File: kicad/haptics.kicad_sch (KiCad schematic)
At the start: 6 parts, among them M401 VG1040003D, U401 DA7280

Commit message: refactor, fix issues, ready for first design
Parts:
- added R504, R505: 10k, symbol Device:R
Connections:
- net PWR: now also R504.1, R505.1
- net SCL: now also R504.2
- net SDA: now also R505.2
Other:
- moved on the sheet: R401

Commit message: essentially finish schematic, start adding footprints, add new footprints
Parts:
- C501: renamed from C401; footprint (none) -> Capacitor_SMD:C_0603_1608Metric_Pad1.08x0.95mm_HandSolder
- R501: renamed from R505; footprint (none) -> Resistor_SMD:R_0603_1608Metric_Pad0.98x0.95mm_HandSolder
- R502: renamed from R504; footprint (none) -> Resistor_SMD:R_0603_1608Metric_Pad0.98x0.95mm_HandSolder
- R503: renamed from R401; footprint (none) -> Resistor_SMD:R_0603_1608Metric_Pad0.98x0.95mm_HandSolder
- TP501: renamed from TP401; footprint (none) -> TestPoint:TestPoint_Pad_D3.0mm
- TP502: renamed from TP402; footprint (none) -> TestPoint:TestPoint_Pad_D3.0mm
- U501: renamed from U401; footprint (none) -> Package_DFN_QFN:QFN-12-1EP_3x3mm_P0.5mm_EP1.65x1.65mm
- renumbered M401 to M501
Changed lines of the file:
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@@
 		(on_board yes)
 		(dnp no)
-		(property "Reference" "TP402"
+		(property "Reference" "TP502"
 			(at 156.972 83.058 90)
 			(effects
@@
 			)
 		)
-		(property "Footprint" ""
+		(property "Footprint" "TestPoint:TestPoint_Pad_D3.0mm"
 			(at 172.72 88.9 0)
 			(effects
@@
 			(project "kicad"
 				(path "/97e37379-fec6-4f0d-82d9-4ea53516bb02/6e1279b2-387a-4a79-8fd5-6fdc8d551df2"
-					(reference "TP402")
+					(reference "TP502")
 					(unit 1)
 				)
@@
 		(on_board yes)
 		(dnp no)
-		(property "Reference" "TP401"
+		(property "Reference" "TP501"
 			(at 156.972 79.248 90)
 			(effects
@@
 			)
 		)
-		(property "Footprint" ""
+		(property "Footprint" "TestPoint:TestPoint_Pad_D3.0mm"
 			(at 172.72 85.09 0)
 			(effects
@@
 			(project "kicad"
 				(path "/97e37379-fec6-4f0d-82d9-4ea53516bb02/6e1279b2-387a-4a79-8fd5-6fdc8d551df2"
-					(reference "TP401")
+					(reference "TP501")
 					(unit 1)
 				)
@@
 		(on_board yes)
 		(dnp no)
-		(property "Reference" "C401"
+		(property "Reference" "C501"
 			(at 114.808 120.65 0)
 			(effects
@@
 			)
 		)
-		(property "Footprint" ""
+		(property "Footprint" "Capacitor_SMD:C_0603_1608Metric_Pad1.08x0.95mm_HandSolder"
 			(at 125.4252 125.73 0)
 			(effects
@@
 			(project "kicad"
 				(path "/97e37379-fec6-4f0d-82d9-4ea53516bb02/6e1279b2-387a-4a79-8fd5-6fdc8d551df2"
-					(reference "C401")
+					(reference "C501")
 					(unit 1)
 				)
@@
 		(on_board yes)
 		(dnp no)
-		(property "Reference" "R505"
+		(property "Reference" "R501"
 			(at 99.06 93.98 0)
 			(effects
@@
 			)
 		)
-		(property "Footprint" ""
+		(property "Footprint" "Resistor_SMD:R_0603_1608Metric_Pad0.98x0.95mm_HandSolder"
 			(at 103.632 95.25 90)
 			(effects
@@
 			(project "kicad"
 				(path "/97e37379-fec6-4f0d-82d9-4ea53516bb02/6e1279b2-387a-4a79-8fd5-6fdc8d551df2"
-					(reference "R505")
+					(reference "R501")
 					(unit 1)
 				)
@@
 		(dnp no)
 		(fields_autoplaced yes)
-		(property "Reference" "#PWR0402"
+		(property "Reference" "#PWR0502"
 			(at 135.89 127 0)
 			(effects
@@
 			(project "kicad"
 				(path "/97e37379-fec6-4f0d-82d9-4ea53516bb02/6e1279b2-387a-4a79-8fd5-6fdc8d551df2"
-					(reference "#PWR0402")
+					(reference "#PWR0502")
 					(unit 1)
 				)
@@
 		(on_board yes)
 		(dnp no)
-		(property "Reference" "R504"
+		(property "Reference" "R502"
 			(at 107.95 91.44 0)
 			(effects
@@
 			)
 		)
-		(property "Footprint" ""
+		(property "Footprint" "Resistor_SMD:R_0603_1608Metric_Pad0.98x0.95mm_HandSolder"
 			(at 112.522 92.71 90)
 			(effects
@@
 			(project "kicad"
 				(path "/97e37379-fec6-4f0d-82d9-4ea53516bb02/6e1279b2-387a-4a79-8fd5-6fdc8d551df2"
-					(reference "R504")
+					(reference "R502")
 					(unit 1)
 				)
@@
 		(dnp no)
 		(fields_autoplaced yes)
-		(property "Reference" "M401"
+		(property "Reference" "M501"
 			(at 154.94 101.5999 0)
 			(effects
@@
 			(project "kicad"
 				(path "/97e37379-fec6-4f0d-82d9-4ea53516bb02/6e1279b2-387a-4a79-8fd5-6fdc8d551df2"
-					(reference "M401")
+					(reference "M501")
 					(unit 1)
 				)
@@
 		(on_board yes)
 		(dnp no)
-		(property "Reference" "R401"
+		(property "Reference" "R503"
 			(at 119.38 87.63 0)
 			(effects
@@
 			)
 		)
-		(property "Footprint" ""
+		(property "Footprint" "Resistor_SMD:R_0603_1608Metric_Pad0.98x0.95mm_HandSolder"
 			(at 123.952 88.9 90)
 			(effects
@@
 			(project "kicad"
 				(path "/97e37379-fec6-4f0d-82d9-4ea53516bb02/6e1279b2-387a-4a79-8fd5-6fdc8d551df2"
-					(reference "R401")
+					(reference "R503")
 					(unit 1)
 				)
@@
 		(on_board yes)
 		(dnp no)
-		(property "Reference" "U401"
+		(property "Reference" "U501"
 			(at 130.81 86.36 0)
 			(effects
@@
 			)
 		)
-		(property "Footprint" ""
+		(property "Footprint" "Package_DFN_QFN:QFN-12-1EP_3x3mm_P0.5mm_EP1.65x1.65mm"
 			(at 128.27 106.68 0)
 			(effects
@@
 			(project "kicad"
 				(path "/97e37379-fec6-4f0d-82d9-4ea53516bb02/6e1279b2-387a-4a79-8fd5-6fdc8d551df2"
-					(reference "U401")
+					(reference "U501")
 					(unit 1)
 				)
@@
 		(dnp no)
 		(fields_autoplaced yes)
-		(property "Reference" "#PWR0401"
+		(property "Reference" "#PWR0501"
 			(at 124.46 132.08 0)
 			(effects
@@
 			(project "kicad"
 				(path "/97e37379-fec6-4f0d-82d9-4ea53516bb02/6e1279b2-387a-4a79-8fd5-6fdc8d551df2"
-					(reference "#PWR0401")
-					(unit 1)
-				)
+					(reference "#PWR0501")
+					(unit 1)
+				)

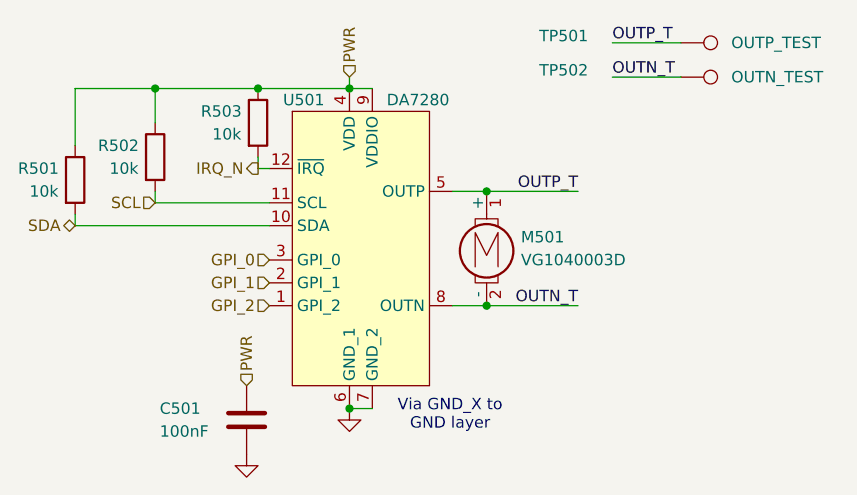
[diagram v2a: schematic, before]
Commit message: fix motor with spring fingers, start PCB
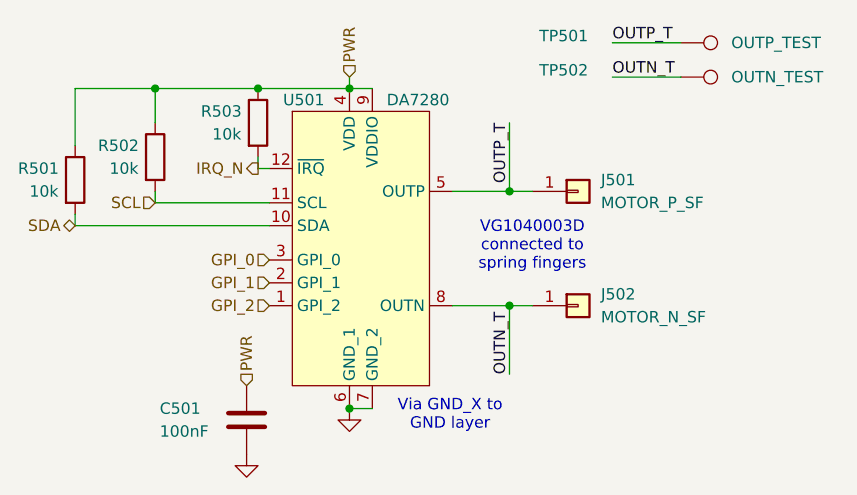
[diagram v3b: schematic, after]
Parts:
- removed M501: VG1040003D, symbol Motor:Motor_DC_ALT
- added J501: MOTOR_P_SF, Raven:TE_2329497-2, symbol Connector_Generic:Conn_01x01
- added J502: MOTOR_N_SF, Raven:TE_2329497-2, symbol Connector_Generic:Conn_01x01
- TP501, TP502: footprint TestPoint:TestPoint_Pad_D3.0mm -> TestPoint:TestPoint_Pad_D1.5mm
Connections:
- net OUTN_T: now also J502.1 (Pin_1)
- net OUTP_T: now also J501.1 (Pin_1)
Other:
- note added: "VG1040003D connected to spring fingers"
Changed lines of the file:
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@@
 	)
 	(junction
-		(at 151.13 109.22)
-		(diameter 0)
-		(color 0 0 0 0)
-	)
-	(junction
-		(at 151.13 96.52)
+		(at 153.67 109.22)
 		(diameter 0)
 		(color 0 0 0 0)
@@
 	)
 	(junction
+		(at 153.67 96.52)
+		(diameter 0)
+		(color 0 0 0 0)
+	)
+	(junction
 		(at 135.89 85.09)
 		(diameter 0)
@@
 	(wire
 		(pts
-			(xy 151.13 109.22) (xy 161.29 109.22)
+			(xy 153.67 109.22) (xy 156.21 109.22)
+		)
+		(stroke
+			(width 0)
+			(type default)
+		)
+	)
+	(wire
+		(pts
+			(xy 153.67 88.9) (xy 153.67 96.52)
 		)
 		(stroke
@@
 	(wire
 		(pts
+			(xy 153.67 109.22) (xy 153.67 116.84)
+		)
+		(stroke
+			(width 0)
+			(type default)
+		)
+	)
+	(wire
+		(pts
 			(xy 135.89 120.65) (xy 138.43 120.65)
 		)
@@
 	(wire
 		(pts
-			(xy 147.32 109.22) (xy 151.13 109.22)
+			(xy 147.32 109.22) (xy 153.67 109.22)
 		)
 		(stroke
@@
 	(wire
 		(pts
-			(xy 147.32 96.52) (xy 151.13 96.52)
+			(xy 147.32 96.52) (xy 153.67 96.52)
 		)
 		(stroke
@@
 	(wire
 		(pts
+			(xy 153.67 96.52) (xy 156.21 96.52)
+		)
+		(stroke
+			(width 0)
+			(type default)
+		)
+	)
+	(wire
+		(pts
 			(xy 105.41 99.06) (xy 105.41 100.33)
 		)
@@
 	(wire
 		(pts
-			(xy 151.13 96.52) (xy 161.29 96.52)
-		)
-		(stroke
-			(width 0)
-			(type default)
-		)
-	)
-	(wire
-		(pts
 			(xy 114.3 88.9) (xy 114.3 85.09)
 		)
@@
 			(width 0)
 			(type default)
+		)
+	)
+	(text "VG1040003D\nconnected to\nspring fingers"
+		(exclude_from_sim no)
+		(at 156.21 102.616 0)
+		(effects
+			(font
+				(size 1.27 1.27)
+			)
 		)
 	)
@@
 	)
 	(label "OUTN_T"
-		(at 161.29 109.22 180)
-		(fields_autoplaced yes)
-		(effects
-			(font
-				(size 1.27 1.27)
-			)
-			(justify right bottom)
+		(at 153.67 116.84 90)
+		(fields_autoplaced yes)
+		(effects
+			(font
+				(size 1.27 1.27)
+			)
+			(justify left bottom)
 		)
 	)
 	(label "OUTP_T"
-		(at 161.29 96.52 180)
+		(at 153.67 88.9 270)
 		(fields_autoplaced yes)
 		(effects
@@
 			)
 			(justify right)
+		)
+	)
+	(symbol
+		(lib_id "Connector_Generic:Conn_01x01")
+		(at 161.29 109.22 0)
+		(unit 1)
+		(exclude_from_sim no)
+		(in_bom yes)
+		(on_board yes)
+		(dnp no)
+		(fields_autoplaced yes)
+		(property "Reference" "J502"
+			(at 163.83 107.9499 0)
+			(effects
+				(font
+					(size 1.27 1.27)
+				)
+				(justify left)
+			)
+		)
+		(property "Value" "MOTOR_N_SF"
+			(at 163.83 110.4899 0)
+			(effects
+				(font
+					(size 1.27 1.27)
+				)
+				(justify left)
+			)
+		)
+		(property "Footprint" "Raven:TE_2329497-2"
+			(at 161.29 109.22 0)
+			(effects
+				(font
+					(size 1.27 1.27)
+				)
+				(hide yes)
+			)
+		)
+		(property "Datasheet" "~"
+			(at 161.29 109.22 0)
+			(effects
+				(font
+					(size 1.27 1.27)
+				)
+				(hide yes)
+			)
+		)
+		(property "Description" "Generic connector, single row, 01x01, script generated (kicad-library-utils/schlib/autogen/connector/)"
+			(at 161.29 109.22 0)
+			(effects
+				(font
+					(size 1.27 1.27)
+				)
+				(hide yes)
+			)
+		)
+		(pin "1"
+		)
+		(instances
+			(project "kicad"
+				(path "/97e37379-fec6-4f0d-82d9-4ea53516bb02/6e1279b2-387a-4a79-8fd5-6fdc8d551df2"
+					(reference "J502")
+					(unit 1)
+				)
+			)
 		)
 	)
@@
 			)
 		)
-		(property "Footprint" "TestPoint:TestPoint_Pad_D3.0mm"
+		(property "Footprint" "TestPoint:TestPoint_Pad_D1.5mm"
 			(at 172.72 88.9 0)
 			(effects
@@
 			)
 		)
-		(property "Footprint" "TestPoint:TestPoint_Pad_D3.0mm"
+		(property "Footprint" "TestPoint:TestPoint_Pad_D1.5mm"
 			(at 172.72 85.09 0)
 			(effects
@@
 	)
 	(symbol
-		(lib_id "Motor:Motor_DC_ALT")
-		(at 151.13 101.6 0)
-		(unit 1)
-		(exclude_from_sim no)
-		(in_bom yes)
-		(on_board yes)
-		(dnp no)
-		(fields_autoplaced yes)
-		(property "Reference" "M501"
-			(at 154.94 101.5999 0)
-			(effects
-				(font
-					(size 1.27 1.27)
-				)
-				(justify left)
-			)
-		)
-		(property "Value" "VG1040003D"
-			(at 154.94 104.1399 0)
-			(effects
-				(font
-					(size 1.27 1.27)
-				)
-				(justify left)
-			)
-		)
-		(property "Footprint" ""
-			(at 151.13 103.886 0)
-			(effects
-				(font
-					(size 1.27 1.27)
-				)
-				(hide yes)
-			)
-		)
-		(property "Datasheet" "~"
-			(at 151.13 103.886 0)
-			(effects
-				(font
-					(size 1.27 1.27)
-				)
-				(hide yes)
-			)
-		)
-		(property "Description" "DC Motor, alternative symbol"
-			(at 151.13 101.6 0)
-			(effects
-				(font
-					(size 1.27 1.27)
-				)
-				(hide yes)
-			)
-		)
-		(pin "2"
-		)
-		(pin "1"
-		)
-		(instances
-			(project "kicad"
-				(path "/97e37379-fec6-4f0d-82d9-4ea53516bb02/6e1279b2-387a-4a79-8fd5-6fdc8d551df2"
-					(reference "M501")
-					(unit 1)
-				)
-			)
-		)
-	)
-	(symbol
 		(lib_id "Device:R")
 		(at 125.73 88.9 0)
@@
 					(unit 1)
 				)
+			)
+		)
+	)
+	(symbol
+		(lib_id "Connector_Generic:Conn_01x01")
+		(at 161.29 96.52 0)
+		(unit 1)
+		(exclude_from_sim no)
+		(in_bom yes)
+		(on_board yes)
+		(dnp no)
+		(fields_autoplaced yes)
+		(property "Reference" "J501"
+			(at 163.83 95.2499 0)
+			(effects
+				(font
+					(size 1.27 1.27)
+				)
+				(justify left)
+			)
+		)
+		(property "Value" "MOTOR_P_SF"
+			(at 163.83 97.7899 0)
+			(effects
+				(font
+					(size 1.27 1.27)
+				)
+				(justify left)
+			)
+		)
+		(property "Footprint" "Raven:TE_2329497-2"
+			(at 161.29 96.52 0)
+			(effects
+				(font
+					(size 1.27 1.27)
+				)
+				(hide yes)
+			)
+		)
+		(property "Datasheet" "~"
+			(at 161.29 96.52 0)
+			(effects
+				(font
+					(size 1.27 1.27)
+				)
+				(hide yes)
+			)
+		)
+		(property "Description" "Generic connector, single row, 01x01, script generated (kicad-library-utils/schlib/autogen/connector/)"
+			(at 161.29 96.52 0)
+			(effects
+				(font
+					(size 1.27 1.27)
+				)
+				(hide yes)
+			)
+		)
+		(pin "1"
+		)
+		(instances
+			(project "kicad"
+				(path "/97e37379-fec6-4f0d-82d9-4ea53516bb02/6e1279b2-387a-4a79-8fd5-6fdc8d551df2"
+					(reference "J501")
+					(unit 1)
+				)

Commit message: fix errors/update USB-c footprint, DA7280 footprint still needs fixing
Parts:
- U501: footprint Package_DFN_QFN:QFN-12-1EP_3x3mm_P0.5mm_EP1.65x1.65mm -> Raven:QFN-12_3x3mm_P0.65mm
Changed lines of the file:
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@@
 			)
 		)
-		(property "Footprint" "Package_DFN_QFN:QFN-12-1EP_3x3mm_P0.5mm_EP1.65x1.65mm"
+		(property "Footprint" "Raven:QFN-12_3x3mm_P0.65mm"
 			(at 128.27 106.68 0)
 			(effects
@@
 		(pin "3"
 		)
+		(pin "13"
+		)
 		(instances

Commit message: PCB almost finished: only battery & usb-c needed
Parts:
- U501: footprint Raven:QFN-12_3x3mm_P0.65mm -> Raven:QFN-12-3x3mm-P0.65mm
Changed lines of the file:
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@@
 			)
 		)
-		(property "Footprint" "Raven:QFN-12_3x3mm_P0.65mm"
+		(property "Footprint" "Raven:QFN-12-3x3mm-P0.65mm"
 			(at 128.27 106.68 0)
 			(effects
@@
 		(pin "3"
 		)
-		(pin "13"
-		)
 		(instances

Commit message: add some assembly files, but transition towards all hand
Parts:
- C501, R501, R502, R503: JLC (none) -> 0603
- J501, J502, TP501, TP502, U501: JLC (none) -> XXXXXX; LCSC (none) -> XXXXXX
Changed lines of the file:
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@@
+			)
+		)
+		(property "JLC" "XXXXXX"
+			(at 161.29 109.22 0)
+			(effects
+				(font
+					(size 1.27 1.27)
+				)
+				(hide yes)
+			)
+		)
+		(property "LCSC" "XXXXXX"
+			(at 161.29 109.22 0)
+			(effects
+				(font
+					(size 1.27 1.27)
+				)
+				(hide yes)
 			)
 		)
@@
 			)
 		)
+		(property "JLC" "XXXXXX"
+			(at 172.72 83.82 0)
+			(effects
+				(font
+					(size 1.27 1.27)
+				)
+				(hide yes)
+			)
+		)
+		(property "LCSC" "XXXXXX"
+			(at 172.72 83.82 0)
+			(effects
+				(font
+					(size 1.27 1.27)
+				)
+				(hide yes)
+			)
+		)
 		(pin "1"
 		)
@@
 			)
 		)
+		(property "JLC" "XXXXXX"
+			(at 172.72 80.01 0)
+			(effects
+				(font
+					(size 1.27 1.27)
+				)
+				(hide yes)
+			)
+		)
+		(property "LCSC" "XXXXXX"
+			(at 172.72 80.01 0)
+			(effects
+				(font
+					(size 1.27 1.27)
+				)
+				(hide yes)
+			)
+		)
 		(pin "1"
 		)
@@
 			)
 		)
+		(property "JLC" "0603"
+			(at 124.46 121.92 0)
+			(effects
+				(font
+					(size 1.27 1.27)
+				)
+				(hide yes)
+			)
+		)
 		(pin "2"
 		)
@@
 		)
 		(property "Description" "Resistor"
+			(at 105.41 95.25 0)
+			(effects
+				(font
+					(size 1.27 1.27)
+				)
+				(hide yes)
+			)
+		)
+		(property "JLC" "0603"
 			(at 105.41 95.25 0)
 			(effects
@@
 			)
 		)
+		(property "JLC" "0603"
+			(at 114.3 92.71 0)
+			(effects
+				(font
+					(size 1.27 1.27)
+				)
+				(hide yes)
+			)
+		)
 		(pin "2"
 		)
@@
 		)
 		(property "Description" "Resistor"
+			(at 125.73 88.9 0)
+			(effects
+				(font
+					(size 1.27 1.27)
+				)
+				(hide yes)
+			)
+		)
+		(property "JLC" "0603"
 			(at 125.73 88.9 0)
 			(effects
@@
 			)
 		)
+		(property "JLC" "XXXXXX"
+			(at 161.29 96.52 0)
+			(effects
+				(font
+					(size 1.27 1.27)
+				)
+				(hide yes)
+			)
+		)
+		(property "LCSC" "XXXXXX"
+			(at 161.29 96.52 0)
+			(effects
+				(font
+					(size 1.27 1.27)
+				)
+				(hide yes)
+			)
+		)
 		(pin "1"
 		)
@@
 			(effects
 				(font
+					(size 1.27 1.27)
+				)
+				(hide yes)
+			)
+		)
+		(property "JLC" "XXXXXX"
+			(at 137.16 101.6 0)
+			(effects
+				(font
+					(size 1.27 1.27)
+				)
+				(hide yes)
+			)
+		)
+		(property "LCSC" "XXXXXX"
+			(at 137.16 101.6 0)
+			(effects
+				(font

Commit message: new battery management w/ separate LDO/charger almost done
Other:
- company: Author: Lucas Merritt -> Mosaic Labs
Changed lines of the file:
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@@
 		(date "2024-09-03")
 		(rev "1")
-		(company "Author: Lucas Merritt")
+		(company "Mosaic Labs")
+		(comment 1 "Lucas Merritt")
 	)
 	(junction

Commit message: Minor revisions for haptics and PCB
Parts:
- removed J501: MOTOR_P_SF, Raven:TE_2329497-2, symbol Connector_Generic:Conn_01x01
- removed J502: MOTOR_N_SF, Raven:TE_2329497-2, symbol Connector_Generic:Conn_01x01
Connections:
- net OUTN_T: no longer names the net of TP502.1, U501.8 (OUTN)
- net OUTP_T: no longer names the net of TP501.1, U501.5 (OUTP)
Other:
- note added: "Motor connected to TPs"
- note removed: "VG1040003D connected to spring fingers"
- moved on the sheet: TP501, TP502
